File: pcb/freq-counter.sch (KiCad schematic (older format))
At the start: 56 parts

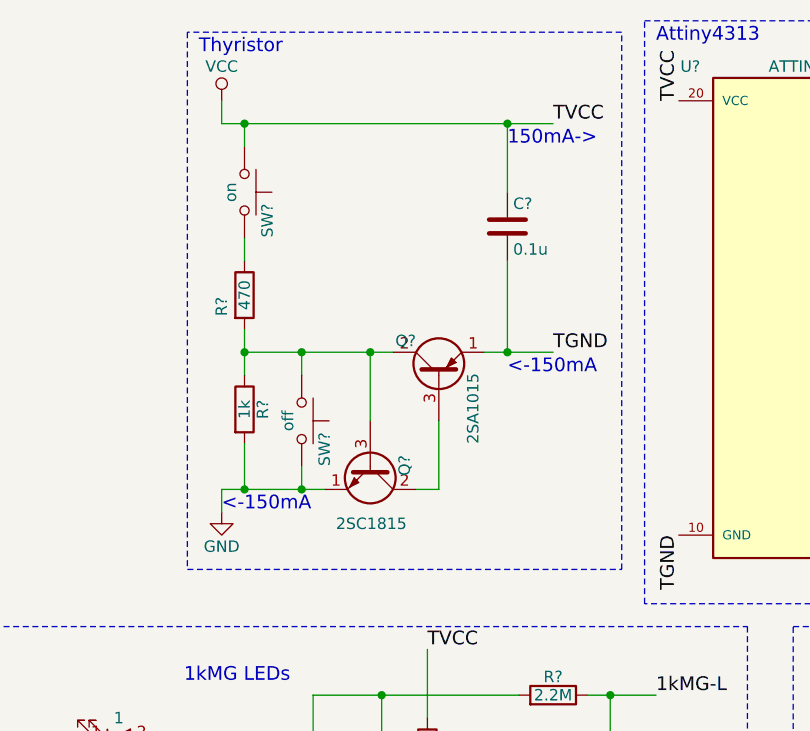
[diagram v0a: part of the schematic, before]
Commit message: delete thyristor.
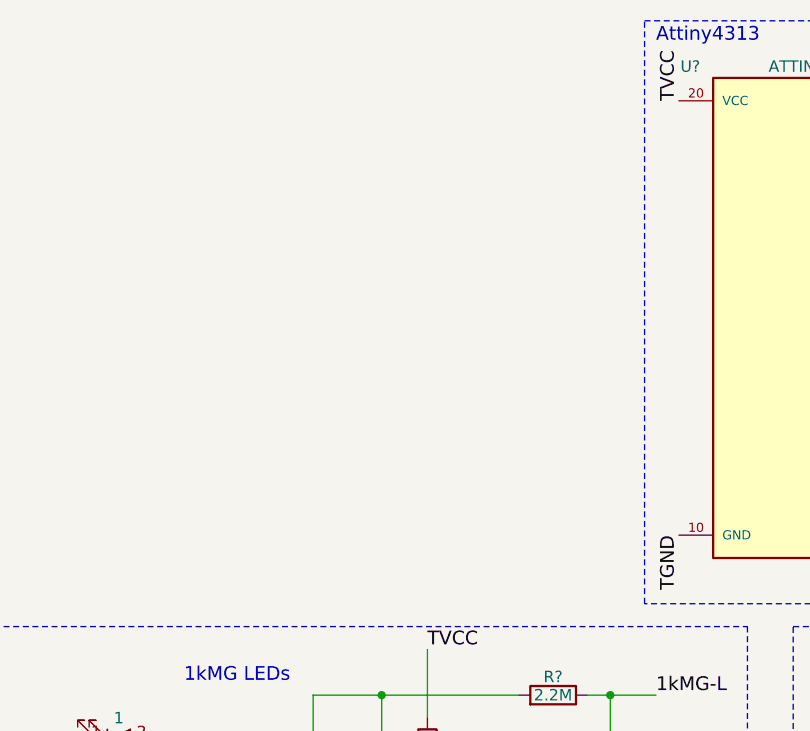
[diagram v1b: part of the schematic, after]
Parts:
- removed C?: 0.1u, symbol C
- removed Q?: 2SC1815, TO_SOT_Packages_THT:TO-92_Molded_Narrow, symbol 2SC1815
- removed Q?: 2SA1015, TO_SOT_Packages_THT:TO-92_Molded_Narrow, symbol 2SA1015
- removed R?: 1k, symbol R
- removed R?: 470, symbol R
- removed SW?: on, symbol SW_Push
- removed SW?: off, symbol SW_Push
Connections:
- net VCC: no longer C?.1, C?.1, C?.1, J?.1 (Pin_1), Q?.1 (E), R?.1, R?.1, R?.2, R?.2, SW?.2, U?.14 (VCC), U?.20 (VCC)
- new net TVCC: C?.1, C?.1, C?.1, J?.1 (Pin_1), Q?.1 (E), R?.1, R?.1, R?.2, R?.2, SW?.2, U?.14 (VCC), U?.20 (VCC)
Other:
- note removed: "150mA->"
- note removed: "<-150mA"
- note removed: "Thyristor"
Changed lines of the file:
@@
 Text Label 8650 1700 0    60   ~ 0
 count-up-1-to-4
-Text Notes 1950 1000 0    60   ~ 0
-Thyristor
-$Comp
-L SW_Push SW?
-U 1 1 5A0DA7E7
-P 2150 1600
-F 0 "SW?" H 2200 1700 50  0000 L CNN
-F 1 "on" H 2150 1540 50  0000 C CNN
-F 2 "" H 2150 1800 50  0001 C CNN
-F 3 "" H 2150 1800 50  0001 C CNN
-	1    2150 1600
-	0    1    1    0
-$EndComp
-$Comp
-L R R?
-U 1 1 5A0DA7E8
-P 2150 2550
-F 0 "R?" V 2230 2550 50  0000 C CNN
-F 1 "1k" V 2150 2550 50  0000 C CNN
-F 2 "" V 2080 2550 50  0001 C CNN
-F 3 "" H 2150 2550 50  0001 C CNN
-	1    2150 2550
-	1    0    0    -1
-$EndComp
-$Comp
-L R R?
-U 1 1 5A0DA7E9
-P 2150 2050
-F 0 "R?" V 2050 2000 50  0000 C CNN
-F 1 "470" V 2150 2050 50  0000 C CNN
-F 2 "" V 2080 2050 50  0001 C CNN
-F 3 "" H 2150 2050 50  0001 C CNN
-	1    2150 2050
-	1    0    0    -1
-$EndComp
-$Comp
-L 2SC1815 Q?
-U 1 1 5A0DA7EA
-P 2700 2800
-F 0 "Q?" H 2650 2950 50  0000 L CNN
-F 1 "2SC1815" V 2950 2650 50  0000 L CNN
-F 2 "TO_SOT_Packages_THT:TO-92_Molded_Narrow" H 2900 2725 50  0001 L CIN
-F 3 "" H 2700 2800 50  0001 L CNN
-	1    2700 2800
-	0    1    1    0
-$EndComp
-$Comp
-L 2SA1015 Q?
-U 1 1 5A0DA7EB
-P 3000 2400
-F 0 "Q?" V 3150 2500 50  0000 L CNN
-F 1 "2SA1015" H 2700 2250 50  0000 L CNN
-F 2 "TO_SOT_Packages_THT:TO-92_Molded_Narrow" H 3200 2325 50  0001 L CIN
-F 3 "" H 3000 2400 50  0001 L CNN
-	1    3000 2400
-	0    -1   -1   0
-$EndComp
-$Comp
-L VCC #PWR?
-U 1 1 5A0DA7ED
-P 2050 1200
-F 0 "#PWR?" H 2050 1050 50  0001 C CNN
-F 1 "VCC" H 2050 1350 50  0000 C CNN
-F 2 "" H 2050 1200 50  0001 C CNN
-F 3 "" H 2050 1200 50  0001 C CNN
-	1    2050 1200
-	1    0    0    -1
-$EndComp
-$Comp
-L GND #PWR?
-U 1 1 5A0DA7EE
-P 2050 3000
-F 0 "#PWR?" H 2050 2750 50  0001 C CNN
-F 1 "GND" H 2050 2850 50  0000 C CNN
-F 2 "" H 2050 3000 50  0001 C CNN
-F 3 "" H 2050 3000 50  0001 C CNN
-	1    2050 3000
-	1    0    0    -1
-$EndComp
-$Comp
-L SW_Push SW?
-U 1 1 5A0DA7F0
-P 2400 2600
-F 0 "SW?" H 2450 2700 50  0000 L CNN
-F 1 "off" H 2400 2540 50  0000 C CNN
-F 2 "" H 2400 2800 50  0001 C CNN
-F 3 "" H 2400 2800 50  0001 C CNN
-	1    2400 2600
-	0    1    1    0
-$EndComp
 $Comp
 L 2SC1815 Q?
@@
 	1    0    0    -1
 $EndComp
-Text Label 3500 1300 0    60   ~ 0
-TVCC
-Text Label 3500 2300 0    60   ~ 0
-TGND
 Text Label 4050 3100 3    60   ~ 0
 TGND
@@
 	1    0    0    -1
 $EndComp
-Text Notes 3300 2400 0    60   ~ 0
-<-150mA
-Text Notes 2050 3000 0    60   ~ 0
-<-150mA
-Text Notes 3300 1400 0    60   ~ 0
-150mA->
 Text Notes 10000 4650 0    60   ~ 0
 10mA
@@
 	1    0    0    -1
 $EndComp
-$Comp
-L C C?
-U 1 1 5A10545C
-P 3300 1750
-F 0 "C?" H 3325 1850 50  0000 L CNN
-F 1 "0.1u" H 3325 1650 50  0000 L CNN
-F 2 "" H 3338 1600 50  0001 C CNN
-F 3 "" H 3300 1750 50  0001 C CNN
-	1    3300 1750
-	1    0    0    -1
-$EndComp
 Text Label 8000 6050 2    60   ~ 0
 TGND
@@
 	6050 4700 6650 4700
 Wire Wire Line
-	3200 2300 3300 2300
-Wire Wire Line
-	3300 2300 3500 2300
-Connection ~ 2700 2300
-Wire Wire Line
-	2700 2300 2700 2600
-Wire Wire Line
-	3000 2900 3000 2600
-Wire Wire Line
-	2900 2900 3000 2900
-Wire Wire Line
 	2050 4300 1750 4300
 Wire Wire Line
@@
 Wire Wire Line
 	10100 3950 10100 4050
-Connection ~ 2400 2900
-Wire Wire Line
-	2400 2900 2400 2800
-Connection ~ 2400 2300
-Wire Wire Line
-	2400 2400 2400 2300
 Connection ~ 8200 6050
 Connection ~ 10550 3950
@@
 	9600 5550 9600 5650
 Wire Notes Line
-	1900 900  1900 3250
-Wire Notes Line
-	3800 900  1900 900
-Wire Notes Line
-	3800 3250 3800 900
-Wire Notes Line
-	1900 3250 3800 3250
-Connection ~ 2150 1300
-Wire Wire Line
-	2050 2900 2050 3000
-Connection ~ 2150 2900
-Wire Wire Line
-	2050 1200 2050 1300
-Wire Wire Line
-	2150 2700 2150 2900
-Wire Wire Line
-	2050 1300 2150 1300
-Wire Wire Line
-	2150 1300 3300 1300
-Wire Wire Line
-	3300 1300 3500 1300
-Wire Wire Line
-	2150 1400 2150 1300
-Wire Wire Line
-	2150 1900 2150 1800
-Connection ~ 2150 2300
-Wire Wire Line
-	2150 2200 2150 2300
-Wire Wire Line
-	2150 2300 2150 2400
-Wire Wire Line
-	2050 2900 2150 2900
-Wire Wire Line
-	2150 2900 2400 2900
-Wire Wire Line
-	2400 2900 2500 2900
-Wire Wire Line
-	2150 2300 2400 2300
-Wire Wire Line
-	2400 2300 2700 2300
-Wire Wire Line
-	2700 2300 2800 2300
-Wire Notes Line
 	11100 3500 7750 3500
 Wire Notes Line
@@
 	5050 5600 5050 5400
 Connection ~ 5050 5400
-Wire Wire Line
-	3300 1300 3300 1600
-Connection ~ 3300 1300
-Wire Wire Line
-	3300 1900 3300 2300
-Connection ~ 3300 2300
 Connection ~ 4850 6000
 Connection ~ 5250 6000

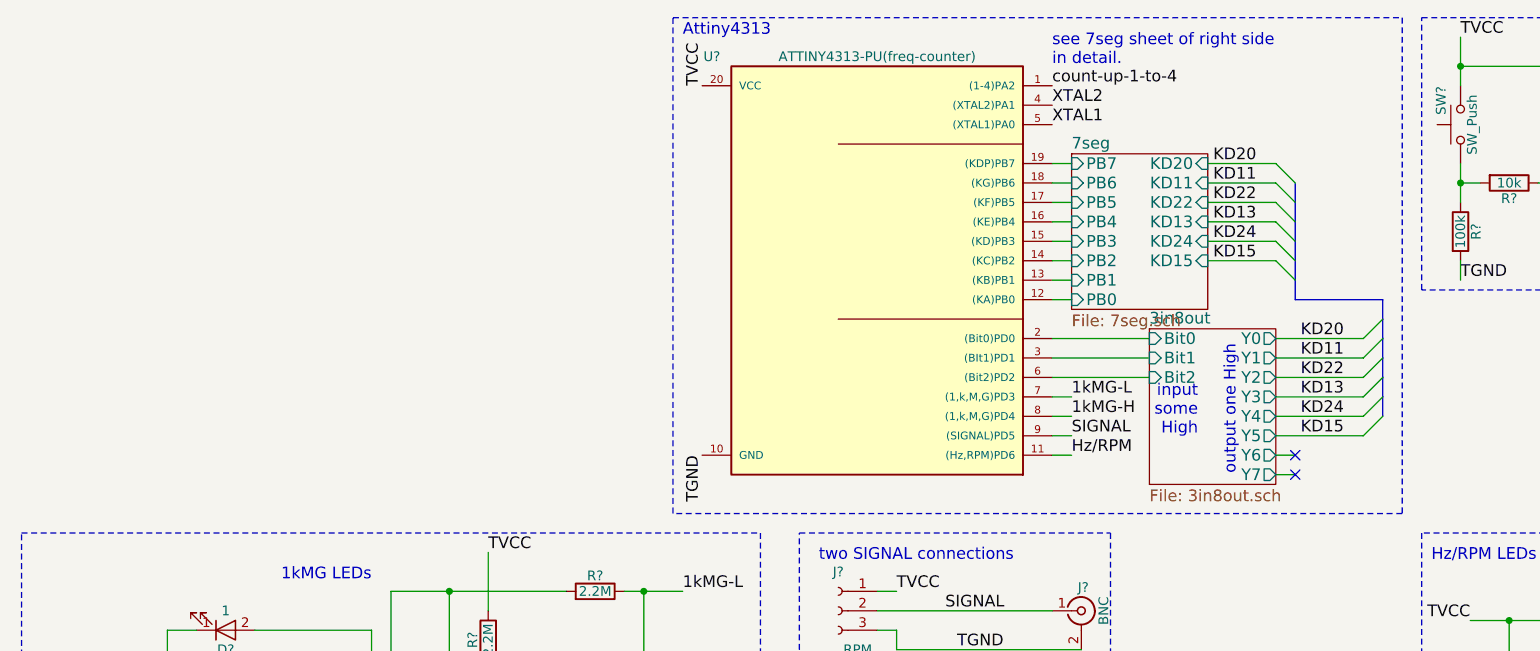
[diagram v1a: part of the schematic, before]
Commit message: add Power part and pass con to Attiny4313 of VCC.
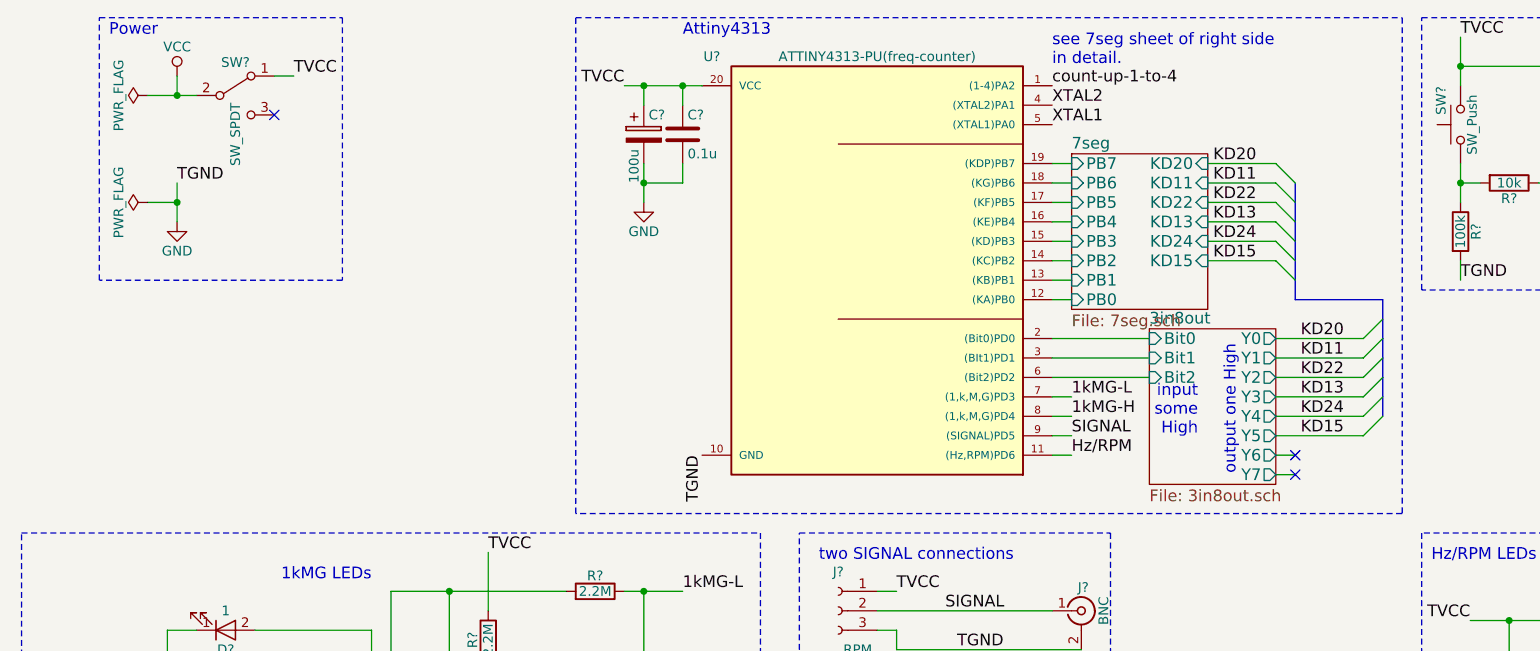
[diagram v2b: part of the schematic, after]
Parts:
- added C?: 100u, symbol CP
- added C?: 0.1u, symbol C
- added SW?: SW_SPDT, symbol SW_SPDT
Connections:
- net TGND is gone; now on net GND: C?.1, C?.2, J?.2 (Ext), J?.3 (Pin_3), Q?.1 (E), Q?.1 (E), Q?.1 (E), Q?.1 (E), R?.1, R?.1, R?.2, R?.2, U?.10 (GND), U?.7 (GND)
- net GND: now also C?.2, C?.2
- net TVCC: now also C?.1, C?.1, SW?.1 (A)
- net VCC: now also SW?.2 (B)
- no-connect marks 2 -> 3
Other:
- note added: "Power"
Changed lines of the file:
@@
 Text Label 4050 3100 3    60   ~ 0
 TGND
-Text Label 4050 1200 1    60   ~ 0
+Text Label 1950 1150 0    60   ~ 0
 TVCC
 Text Label 5950 2800 0    60   ~ 0
@@
 	7950 2100 7950 2200
 Wire Notes Line
-	7650 3400 3900 3400
-Wire Notes Line
-	3900 3400 3900 850
-Wire Notes Line
-	3900 850  7650 850
+	7650 3400 3400 3400
+Wire Notes Line
+	3400 3400 3400 850
+Wire Notes Line
+	3400 850  7650 850
 Wire Notes Line
 	7650 850  7650 3400
@@
 Connection ~ 1300 5600
 Connection ~ 1300 4300
+$Comp
+L SW_SPDT SW?
+U 1 1 5A148FCD
+P 1650 1250
+F 0 "SW?" H 1650 1420 50  0000 C CNN
+F 1 "SW_SPDT" V 1650 1050 50  0000 C CNN
+F 2 "" H 1650 1250 50  0001 C CNN
+F 3 "" H 1650 1250 50  0001 C CNN
+	1    1650 1250
+	1    0    0    -1
+$EndComp
+$Comp
+L VCC #PWR?
+U 1 1 5A149A89
+P 1350 1150
+F 0 "#PWR?" H 1350 1000 50  0001 C CNN
+F 1 "VCC" H 1350 1300 50  0000 C CNN
+F 2 "" H 1350 1150 50  0001 C CNN
+F 3 "" H 1350 1150 50  0001 C CNN
+	1    1350 1150
+	1    0    0    -1
+$EndComp
+Text Label 3650 1200 2    60   ~ 0
+TVCC
+Wire Wire Line
+	3650 1200 3750 1200
+Wire Wire Line
+	3750 1200 3950 1200
+Wire Wire Line
+	3950 1200 4050 1200
+Wire Wire Line
+	1200 1250 1350 1250
+Wire Wire Line
+	1350 1250 1450 1250
+Wire Wire Line
+	1350 1250 1350 1150
+NoConn ~ 1850 1350
+$Comp
+L GND #PWR?
+U 1 1 5A14ACE7
+P 1350 1900
+F 0 "#PWR?" H 1350 1650 50  0001 C CNN
+F 1 "GND" H 1350 1750 50  0000 C CNN
+F 2 "" H 1350 1900 50  0001 C CNN
+F 3 "" H 1350 1900 50  0001 C CNN
+	1    1350 1900
+	1    0    0    -1
+$EndComp
+Text Label 1350 1700 0    60   ~ 0
+TGND
+Wire Wire Line
+	1350 1700 1350 1800
+Wire Wire Line
+	1350 1800 1350 1900
+$Comp
+L PWR_FLAG #FLG?
+U 1 1 5A14B084
+P 1200 1800
+F 0 "#FLG?" H 1200 1875 50  0001 C CNN
+F 1 "PWR_FLAG" H 1200 1950 50  0000 C CNN
+F 2 "" H 1200 1800 50  0001 C CNN
+F 3 "" H 1200 1800 50  0001 C CNN
+	1    1200 1800
+	0    -1   -1   0
+$EndComp
+Wire Wire Line
+	1200 1800 1350 1800
+Connection ~ 1350 1800
+$Comp
+L PWR_FLAG #FLG?
+U 1 1 5A14B889
+P 1200 1250
+F 0 "#FLG?" H 1200 1325 50  0001 C CNN
+F 1 "PWR_FLAG" H 1200 1400 50  0000 C CNN
+F 2 "" H 1200 1250 50  0001 C CNN
+F 3 "" H 1200 1250 50  0001 C CNN
+	1    1200 1250
+	0    -1   -1   0
+$EndComp
+Connection ~ 1350 1250
+$Comp
+L CP C?
+U 1 1 5A14CF46
+P 3750 1450
+F 0 "C?" H 3775 1550 50  0000 L CNN
+F 1 "100u" V 3700 1200 50  0000 L CNN
+F 2 "" H 3788 1300 50  0001 C CNN
+F 3 "" H 3750 1450 50  0001 C CNN
+	1    3750 1450
+	1    0    0    -1
+$EndComp
+$Comp
+L GND #PWR?
+U 1 1 5A14CF4C
+P 3750 1800
+F 0 "#PWR?" H 3750 1550 50  0001 C CNN
+F 1 "GND" H 3750 1650 50  0000 C CNN
+F 2 "" H 3750 1800 50  0001 C CNN
+F 3 "" H 3750 1800 50  0001 C CNN
+	1    3750 1800
+	1    0    0    -1
+$EndComp
+$Comp
+L C C?
+U 1 1 5A14CF52
+P 3950 1450
+F 0 "C?" H 3975 1550 50  0000 L CNN
+F 1 "0.1u" H 3975 1350 50  0000 L CNN
+F 2 "" H 3988 1300 50  0001 C CNN
+F 3 "" H 3950 1450 50  0001 C CNN
+	1    3950 1450
+	1    0    0    -1
+$EndComp
+Wire Wire Line
+	3750 1200 3750 1300
+Wire Wire Line
+	3750 1600 3750 1700
+Wire Wire Line
+	3750 1700 3750 1800
+Wire Wire Line
+	3950 1200 3950 1300
+Wire Wire Line
+	3950 1600 3950 1700
+Wire Wire Line
+	3950 1700 3750 1700
+Connection ~ 3750 1700
+Connection ~ 3950 1200
+Connection ~ 3750 1200
+Wire Notes Line
+	950  850  2200 850
+Wire Notes Line
+	2200 850  2200 2200
+Wire Notes Line
+	2200 2200 950  2200
+Wire Notes Line
+	950  2200 950  850
+Text Notes 1000 950  0    60   ~ 0
+Power
+Wire Wire Line
+	1950 1150 1850 1150
 $EndSCHEMATC

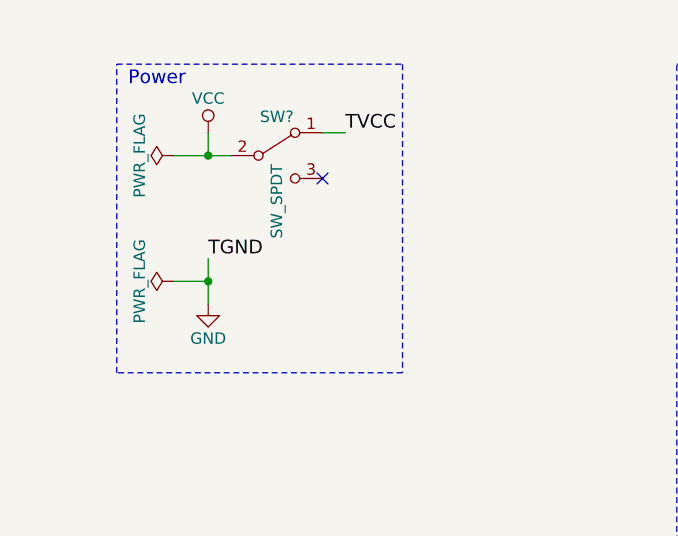
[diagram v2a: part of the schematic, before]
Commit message: add global label of "TVCC" in Power part.
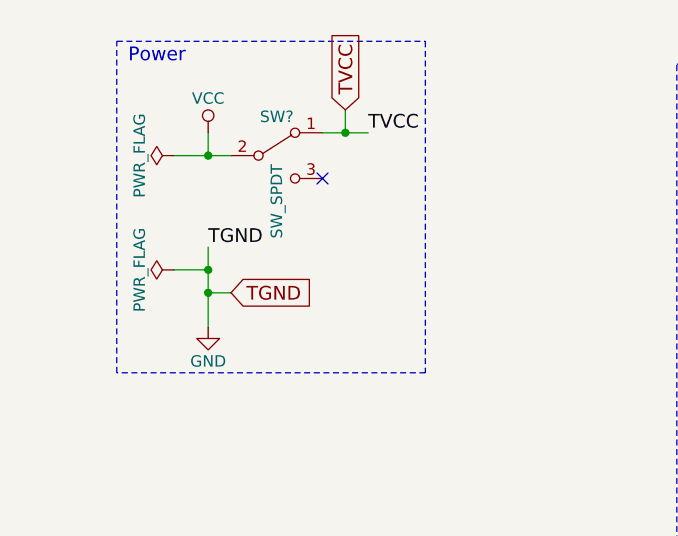
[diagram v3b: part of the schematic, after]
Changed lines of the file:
@@
 Text Label 4050 3100 3    60   ~ 0
 TGND
-Text Label 1950 1150 0    60   ~ 0
+Text Label 2050 1150 0    60   ~ 0
 TVCC
 Text Label 5950 2800 0    60   ~ 0
@@
 L GND #PWR?
 U 1 1 5A14ACE7
-P 1350 1900
-F 0 "#PWR?" H 1350 1650 50  0001 C CNN
-F 1 "GND" H 1350 1750 50  0000 C CNN
-F 2 "" H 1350 1900 50  0001 C CNN
-F 3 "" H 1350 1900 50  0001 C CNN
-	1    1350 1900
-	1    0    0    -1
-$EndComp
-Text Label 1350 1700 0    60   ~ 0
-TGND
-Wire Wire Line
-	1350 1700 1350 1800
-Wire Wire Line
-	1350 1800 1350 1900
+P 1350 2000
+F 0 "#PWR?" H 1350 1750 50  0001 C CNN
+F 1 "GND" H 1350 1850 50  0000 C CNN
+F 2 "" H 1350 2000 50  0001 C CNN
+F 3 "" H 1350 2000 50  0001 C CNN
+	1    1350 2000
+	1    0    0    -1
+$EndComp
+Text Label 1350 1650 0    60   ~ 0
+TGND
+Wire Wire Line
+	1350 1650 1350 1750
+Wire Wire Line
+	1350 1750 1350 1850
+Wire Wire Line
+	1350 1850 1350 2000
 $Comp
 L PWR_FLAG #FLG?
 U 1 1 5A14B084
-P 1200 1800
-F 0 "#FLG?" H 1200 1875 50  0001 C CNN
-F 1 "PWR_FLAG" H 1200 1950 50  0000 C CNN
-F 2 "" H 1200 1800 50  0001 C CNN
-F 3 "" H 1200 1800 50  0001 C CNN
-	1    1200 1800
+P 1200 1750
+F 0 "#FLG?" H 1200 1825 50  0001 C CNN
+F 1 "PWR_FLAG" H 1200 1900 50  0000 C CNN
+F 2 "" H 1200 1750 50  0001 C CNN
+F 3 "" H 1200 1750 50  0001 C CNN
+	1    1200 1750
 	0    -1   -1   0
 $EndComp
 Wire Wire Line
-	1200 1800 1350 1800
-Connection ~ 1350 1800
+	1200 1750 1350 1750
+Connection ~ 1350 1750
 $Comp
 L PWR_FLAG #FLG?
@@
 Connection ~ 3750 1200
 Wire Notes Line
-	950  850  2200 850
-Wire Notes Line
-	2200 850  2200 2200
-Wire Notes Line
-	2200 2200 950  2200
-Wire Notes Line
-	950  2200 950  850
-Text Notes 1000 950  0    60   ~ 0
+	950  750  2300 750
+Wire Notes Line
+	2300 750  2300 2200
+Wire Notes Line
+	2300 2200 950  2200
+Wire Notes Line
+	950  2200 950  750
+Text Notes 1000 850  0    60   ~ 0
 Power
 Wire Wire Line
-	1950 1150 1850 1150
+	1850 1150 1950 1150
+Wire Wire Line
+	1950 1150 2050 1150
+Text GLabel 1950 1050 1    60   Input ~ 0
+TVCC
+Wire Wire Line
+	1950 1050 1950 1150
+Connection ~ 1950 1150
+Text GLabel 1450 1850 2    60   Input ~ 0
+TGND
+Wire Wire Line
+	1450 1850 1350 1850
+Connection ~ 1350 1850
 $EndSCHEMATC

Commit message: annotate.
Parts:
- gave numbers to parts that had none: 52
